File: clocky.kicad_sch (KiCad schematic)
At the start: 83 parts, among them J1 Bot 50 pin, J2 Bot 40 pin, J3 Top 50 pin, J4 Top 40 pin, J5 Power, J6 JST_PH, J8 Program, U1 HEF4094B, U10 TMP117xxDRV, U2 HEF4094B, U3 HEF4094B, U4 HEF4094B, U5 HEF4094B, U6 HEF4094B, U7 BQ25570, U9 STM32U031C8Ux, Y1 32768Hz

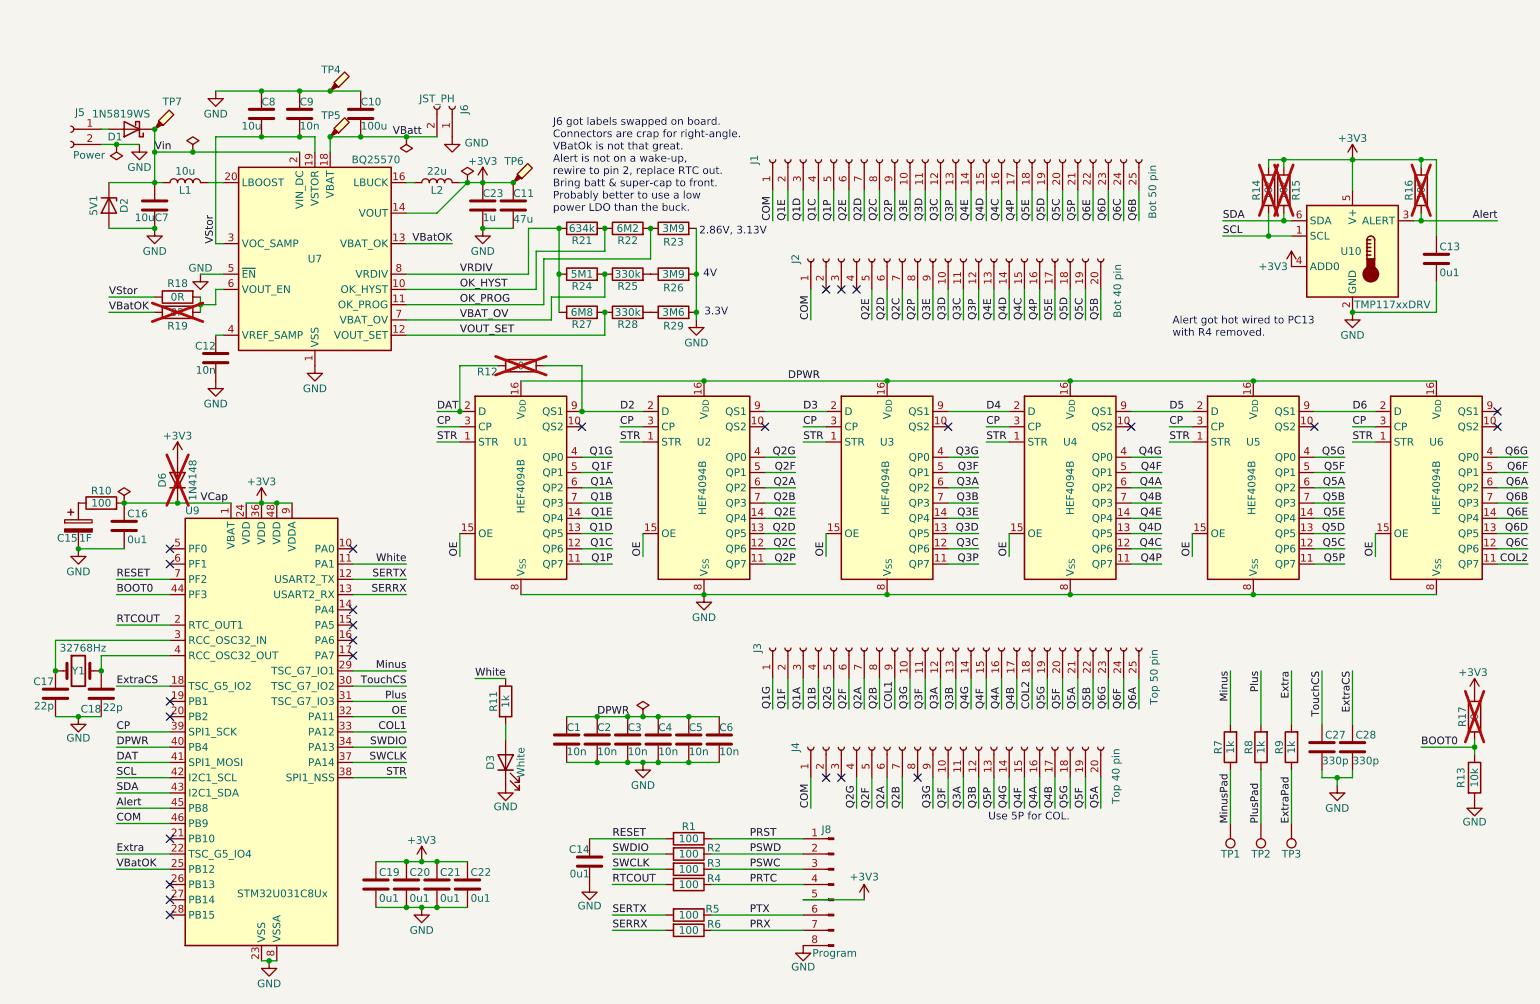
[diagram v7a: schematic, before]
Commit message: Update schematic with pressure and humidity.
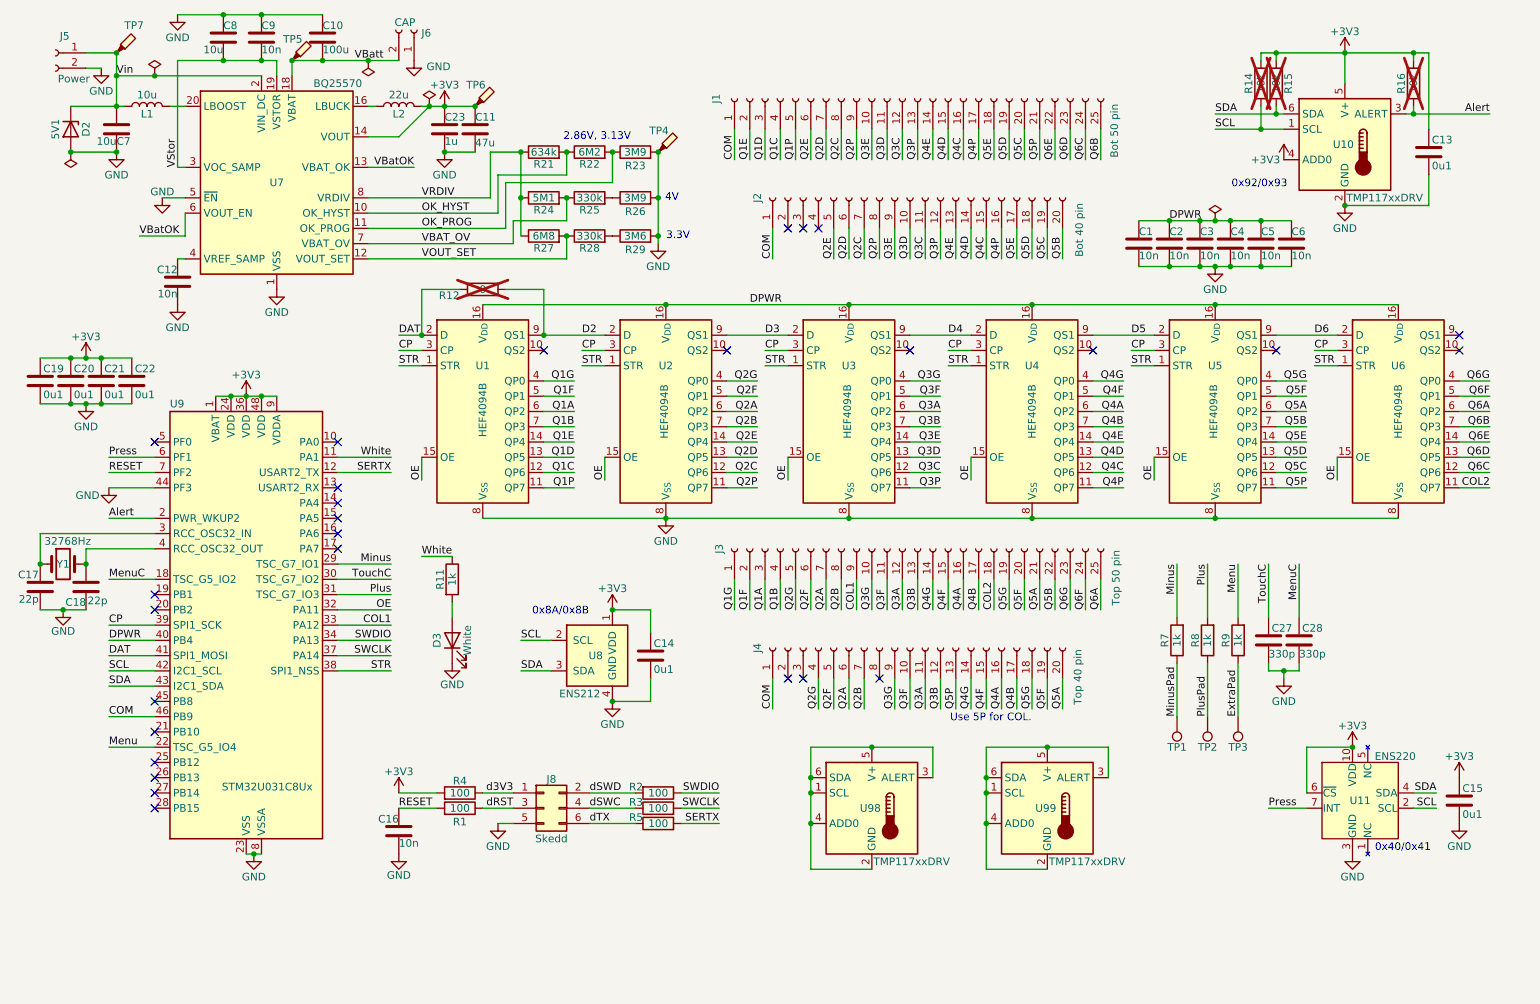
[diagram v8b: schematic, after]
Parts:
- removed C15: 1F, Capacitor_THT:C_Radial_D8.0mm_H11.5mm_P3.50mm, symbol Device:C_Polarized
- removed D1: 1N5819WS, Diode_SMD:D_SOD-323, symbol Diode:1N5819WS
- removed D6: 1N4148, Diode_SMD:D_0603_1608Metric, symbol Device:D
- removed J8: Program, Parts:PinHeader_1x08_P2.54mm_Vertical, symbol Connector:Conn_01x08_Pin
- removed R10: 100, Resistor_SMD:R_0603_1608Metric, symbol Device:R
- removed R13: 10k, Resistor_SMD:R_0402_1005Metric, symbol Device:R
- removed R17: 0, Resistor_SMD:R_0603_1608Metric, symbol Device:R
- removed R18, R19: 0R, Resistor_SMD:R_0603_1608Metric, symbol Device:R
- removed R6: 100, Resistor_SMD:R_0402_1005Metric, symbol Device:R
- added C15: 0u1, Capacitor_SMD:C_0402_1005Metric, symbol Device:C
- added J8: Skedd, Parts:Skedd6, symbol Connector_Generic:Conn_02x03_Odd_Even
- added U11: ENS220, Parts:ENS220, symbol Parts:ENS220
- added U8: ENS212, Package_DFN_QFN:AMS_QFN-4-1EP_2x2mm_P0.95mm_EP0.7x1.6mm, symbol Sensor_Humidity:ENS210
- added U98, U99: TMP117xxDRV, Parts:WSON-6-1EP_2x2mm_P0.65mm_NoEP, symbol Sensor_Temperature:TMP117xxDRV
- C16: value 0u1 -> 10n; JLCPCB C307331 -> (none); LCSC (none) -> C15195
- J6: value JST_PH -> CAP; footprint Connector_JST:JST_PH_B2B-PH-K_1x02_P2.00mm_Vertical -> Parts:TwoPin_P3.5mm
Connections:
- net BOOT0 is gone; now on net GND: U9.44 (PF3)
- net PSWD is gone; now on net SWDIO: R2.1
- net +3V3: now also C14.1, R4.2, U9.1 (VBAT), C15.1, U11.10 (VDD), U11.6 (~{CS}), U8.1 (VDD)
- net Alert: now also U9.2 (PC13); no longer U9.45 (PB8)
- net GND: now also C15.2, J8.5 (Pin_5), U11.3 (GND), U11.8 (GND), U11.9 (GND), U8.4 (GND), U8.5 (GND)
- net RESET: now also C16.1; no longer C14.1
- net SCL: now also U11.2 (SCL), U8.2 (SCL)
- net SDA: now also U11.4 (SDA), U8.3 (SDA)
- net SWDIO: no longer R2.2
- net VBatOK: now also U7.6 (VOUT_EN); no longer U9.25 (PB12)
- net Vin: now also J5.1 (Pin_1)
- net Press: now reaches U9.6 (PF1)
- net Press: now also U11.7 (INT)
- net Extra renamed Menu
- net ExtraCS renamed MenuC
- net PRST renamed dRST
- net dRST: now also J8.3 (Pin_3)
- net PRTC renamed d3V3
- net d3V3: now also J8.1 (Pin_1)
- net PSWC renamed dSWC
- net dSWC: now also J8.4 (Pin_4)
- net PTX renamed dTX
- net dTX: now also J8.6 (Pin_6)
- removed net RTCOUT: R4.2, U9.2 (PC13)
- net SERRX: no longer names the net of U9.13 (PA3)
- net TouchCS renamed TouchC
- removed net VCap: C16.1, U9.1 (VBAT)
- new net: U99.1 (SCL), U99.2 (GND), U99.3 (ALERT), U99.4 (ADD0), U99.5 (V+), U99.6 (SDA)
- new net: U98.1 (SCL), U98.2 (GND), U98.3 (ALERT), U98.4 (ADD0), U98.5 (V+), U98.6 (SDA)
- new net dSWD: J8.2 (Pin_2), R2.2
- no-connect marks 26 -> 28
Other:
- note added: "0x40/0x41"
- note added: "0x8A/0x8B"
- note added: "0x92/0x93"
- note removed: "Alert got hot wired to PC13 with R4 removed."
- note removed: "J6 got labels swapped on board. Connectors are crap for right-angle. VBatOk is not that great. Alert is not on a wake-up, rewire to pin 2, replace RTC out. Bring batt & super-cap to front. Probably better to use a low power LDO than the buck."
- moved on the sheet: C1, C10, C11, C12, C13, C17, C18, C19, C2, C20, C21, C22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
